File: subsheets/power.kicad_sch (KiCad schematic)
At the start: 27 parts

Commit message: Added MCU sch sheet and updated sheet layout
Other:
- company: (none) -> University of Central Florida
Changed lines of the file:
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@@
 (kicad_sch (version 20210621) (generator eeschema)
   (paper "A4")
-  (junction (at 172.72 55.88) (diameter 0) (color 0 0 0 0))
+  (title_block
+    (company "University of Central Florida")
+    (comment 1 "Randy Alvarez")
+    (comment 2 "Parke Benjamin")
+  )
+  (junction (at 115.57 62.23) (diameter 0) (color 0 0 0 0))
+  (junction (at 147.32 139.7) (diameter 0) (color 0 0 0 0))
+  (junction (at 69.85 72.39) (diameter 0) (color 0 0 0 0))
+  (junction (at 139.7 128.27) (diameter 0) (color 0 0 0 0))
+  (junction (at 115.57 88.9) (diameter 0) (color 0 0 0 0))
+  (junction (at 172.72 66.04) (diameter 0) (color 0 0 0 0))
   (junction (at 99.06 53.34) (diameter 0) (color 0 0 0 0))
-  (junction (at 172.72 66.04) (diameter 0) (color 0 0 0 0))
-  (junction (at 167.64 88.9) (diameter 0) (color 0 0 0 0))
+  (junction (at 113.03 88.9) (diameter 0) (color 0 0 0 0))
+  (junction (at 120.65 109.22) (diameter 0) (color 0 0 0 0))
+  (junction (at 77.47 72.39) (diameter 0) (color 0 0 0 0))
   (junction (at 91.44 53.34) (diameter 0) (color 0 0 0 0))
   (junction (at 186.69 88.9) (diameter 0) (color 0 0 0 0))
-  (junction (at 120.65 109.22) (diameter 0) (color 0 0 0 0))
+  (junction (at 167.64 88.9) (diameter 0) (color 0 0 0 0))
+  (junction (at 69.85 74.93) (diameter 0) (color 0 0 0 0))
   (junction (at 113.03 101.6) (diameter 0) (color 0 0 0 0))
-  (junction (at 115.57 88.9) (diameter 0) (color 0 0 0 0))
-  (junction (at 113.03 88.9) (diameter 0) (color 0 0 0 0))
-  (junction (at 139.7 128.27) (diameter 0) (color 0 0 0 0))
-  (junction (at 147.32 139.7) (diameter 0) (color 0 0 0 0))
-  (junction (at 77.47 72.39) (diameter 0) (color 0 0 0 0))
-  (junction (at 69.85 74.93) (diameter 0) (color 0 0 0 0))
+  (junction (at 165.1 58.42) (diameter 0) (color 0 0 0 0))
   (junction (at 120.65 114.3) (diameter 0) (color 0 0 0 0))
-  (junction (at 69.85 72.39) (diameter 0) (color 0 0 0 0))
+  (junction (at 172.72 55.88) (diameter 0) (color 0 0 0 0))
   (junction (at 217.17 55.88) (diameter 0) (color 0 0 0 0))
-  (junction (at 165.1 58.42) (diameter 0) (color 0 0 0 0))
-  (junction (at 115.57 62.23) (diameter 0) (color 0 0 0 0))
   (wire (pts (xy 59.69 77.47) (xy 57.15 77.47))
     (stroke (width 0) (type default) (color 0 0 0 0))

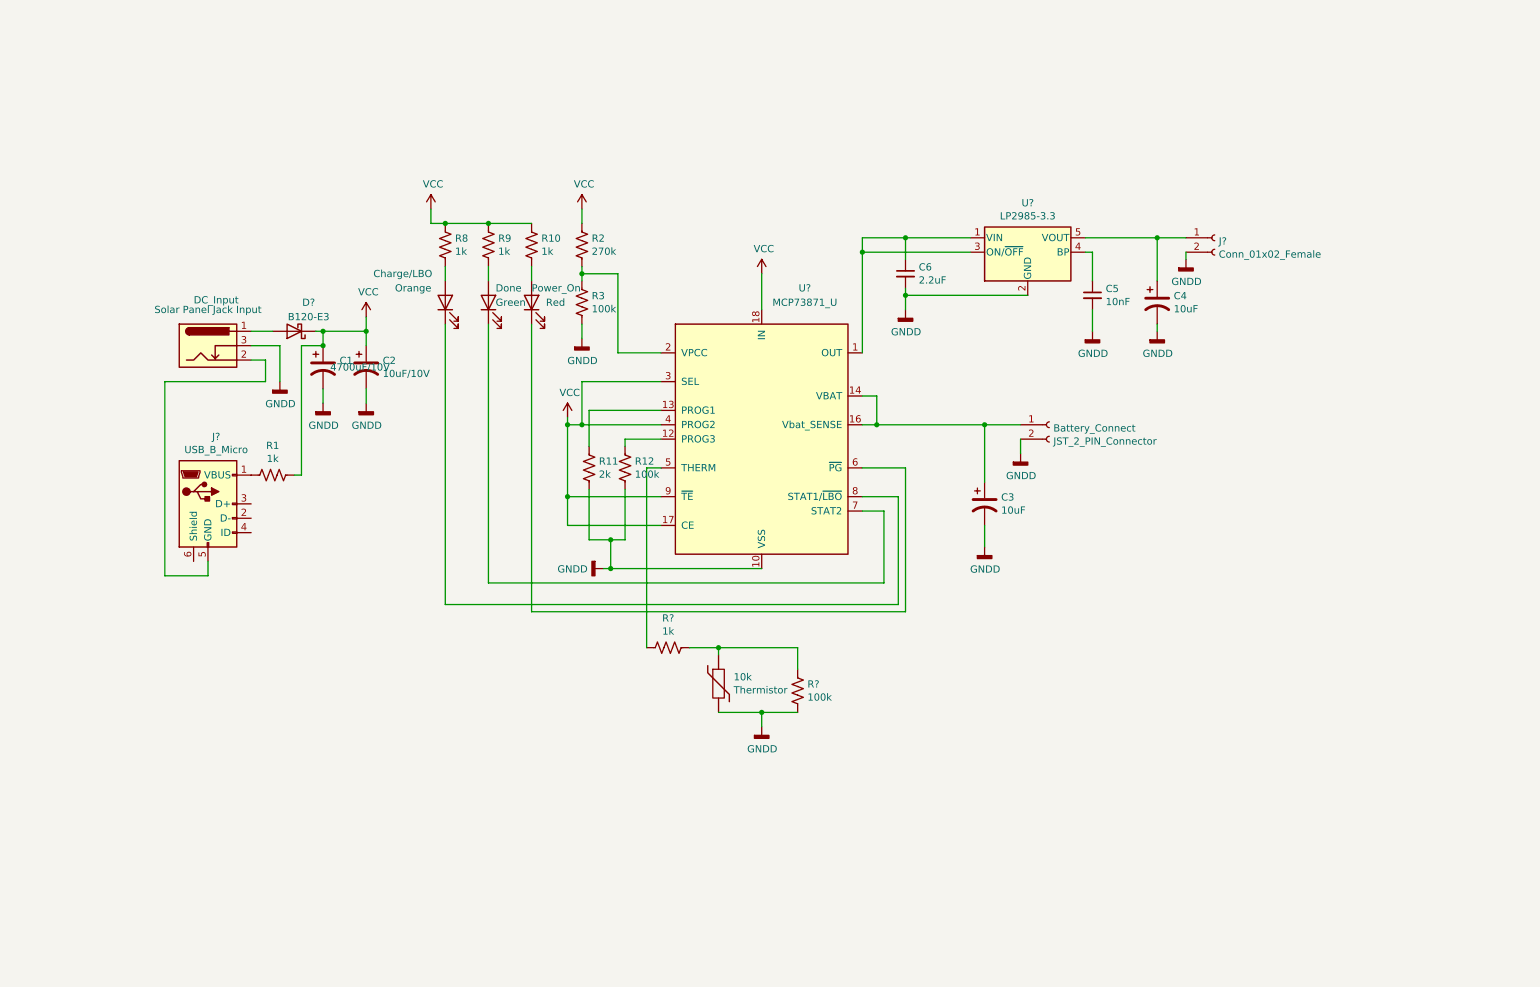
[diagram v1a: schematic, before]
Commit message: Created Sensor Library
- Added Bosch BME688, SPS30, ZMOD symbols to MCU schematic
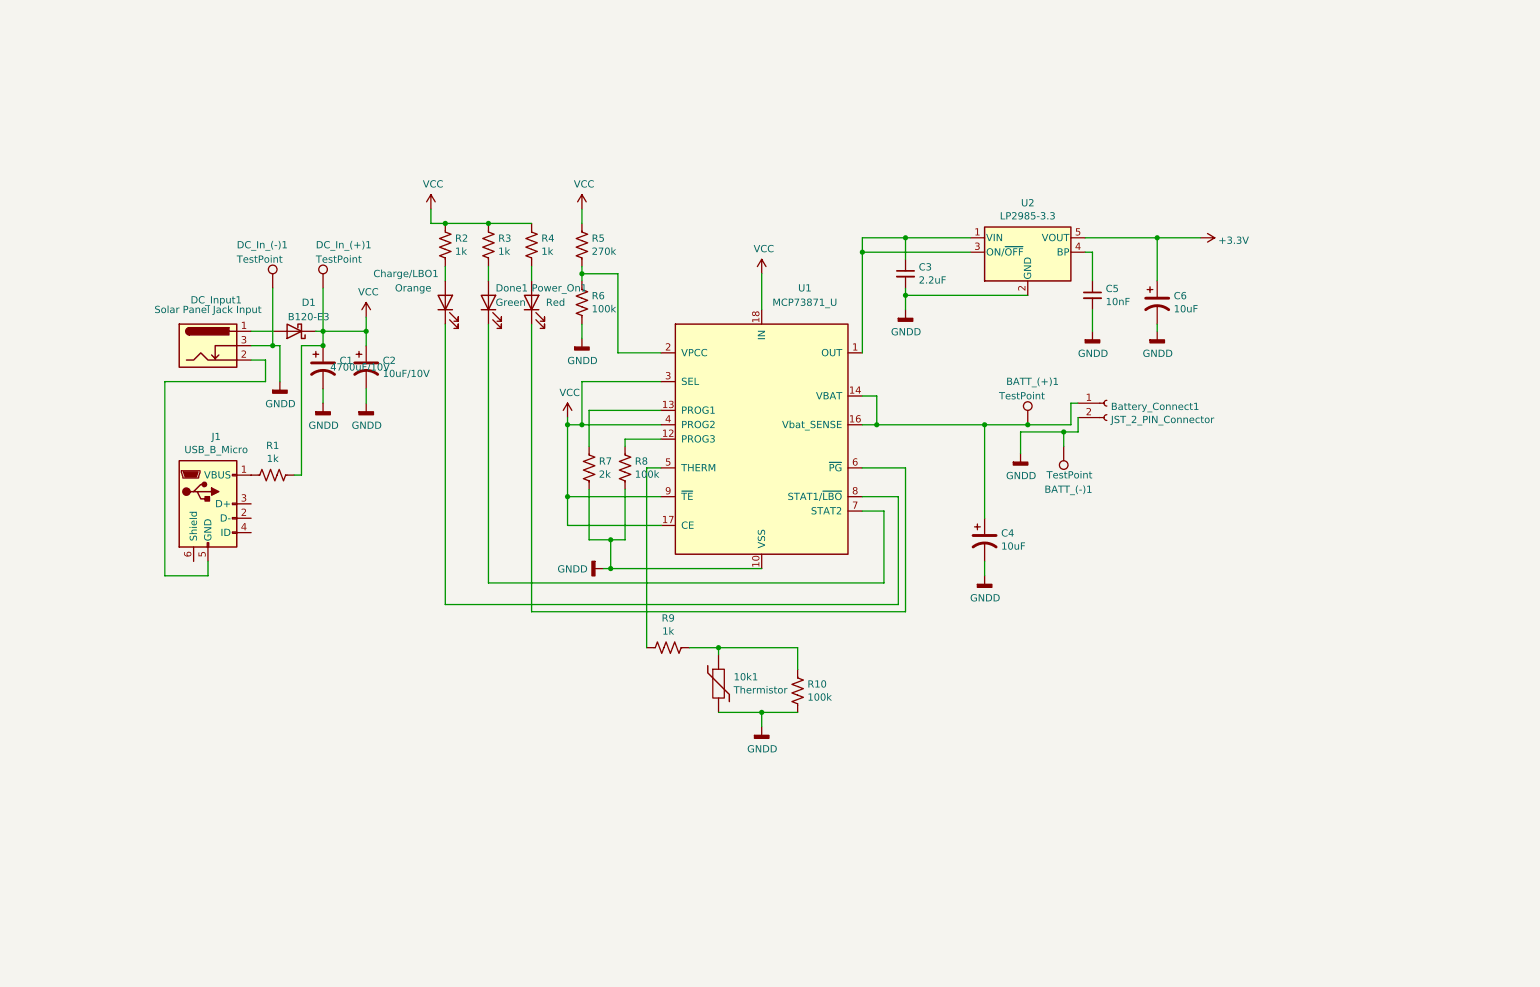
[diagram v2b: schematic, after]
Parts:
- removed J?: Conn_01x02_Female, symbol Connector:Conn_01x02_Female
- added BATT_(+)1, BATT_(-)1, DC_In_(+)1, DC_In_(-)1: TestPoint, symbol Connector:TestPoint
- gave numbers to parts that had none: 6
- renumbered 10k to 10k1, Battery_Connect to Battery_Connect1, C6 to C3, C3 to C4, C4 to C6, Charge/LBO to Charge/LBO1, DC_Input to DC_Input1, Done to Done1, Power_On to Power_On1, R8 to R2, R9 to R3, R10 to R4, R2 to R5, R3 to R6, R11 to R7, R12 to R8
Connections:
- net GNDD: now also BATT_(-)1.1, DC_In_(-)1.1
- net VCC: now also DC_In_(+)1.1
- net at Battery_Connect1.1 (Pin_1), C4.1, U1.14 (VBAT)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: now also BATT_(+)1.1
- net +3V3: now reaches C6.1, U2.5 (VOUT)
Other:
- moved on the sheet: Battery_Connect1, C4

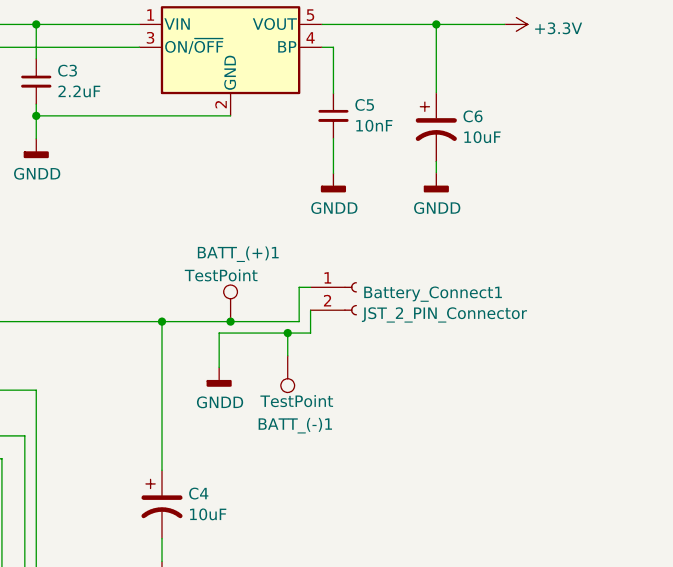
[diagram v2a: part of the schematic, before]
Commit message: Connected ZMOD and Bosch Sensors
-
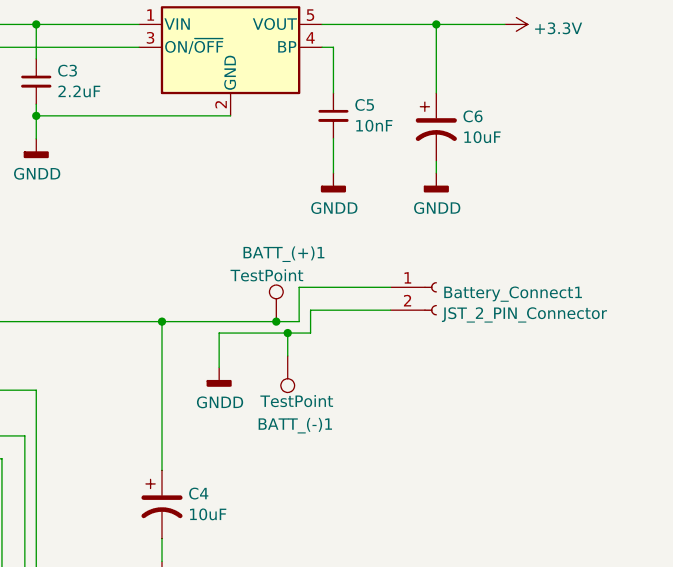
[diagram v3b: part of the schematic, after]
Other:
- moved on the sheet: BATT_(+)1, Battery_Connect1
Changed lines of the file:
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@@
     (comment 2 "Parke Benjamin")
   )
+  (junction (at 120.65 114.3) (diameter 0) (color 0 0 0 0))
+  (junction (at 69.85 72.39) (diameter 0) (color 0 0 0 0))
+  (junction (at 113.03 88.9) (diameter 0) (color 0 0 0 0))
+  (junction (at 200.66 90.17) (diameter 0) (color 0 0 0 0))
+  (junction (at 120.65 109.22) (diameter 0) (color 0 0 0 0))
+  (junction (at 115.57 62.23) (diameter 0) (color 0 0 0 0))
+  (junction (at 99.06 53.34) (diameter 0) (color 0 0 0 0))
+  (junction (at 115.57 88.9) (diameter 0) (color 0 0 0 0))
+  (junction (at 167.64 88.9) (diameter 0) (color 0 0 0 0))
+  (junction (at 77.47 72.39) (diameter 0) (color 0 0 0 0))
   (junction (at 69.85 74.93) (diameter 0) (color 0 0 0 0))
-  (junction (at 113.03 88.9) (diameter 0) (color 0 0 0 0))
-  (junction (at 217.17 55.88) (diameter 0) (color 0 0 0 0))
-  (junction (at 69.85 72.39) (diameter 0) (color 0 0 0 0))
+  (junction (at 172.72 55.88) (diameter 0) (color 0 0 0 0))
+  (junction (at 113.03 101.6) (diameter 0) (color 0 0 0 0))
   (junction (at 172.72 66.04) (diameter 0) (color 0 0 0 0))
-  (junction (at 115.57 88.9) (diameter 0) (color 0 0 0 0))
-  (junction (at 139.7 128.27) (diameter 0) (color 0 0 0 0))
-  (junction (at 120.65 109.22) (diameter 0) (color 0 0 0 0))
-  (junction (at 200.66 90.17) (diameter 0) (color 0 0 0 0))
-  (junction (at 172.72 55.88) (diameter 0) (color 0 0 0 0))
+  (junction (at 186.69 88.9) (diameter 0) (color 0 0 0 0))
+  (junction (at 199.39 88.9) (diameter 0) (color 0 0 0 0))
   (junction (at 165.1 58.42) (diameter 0) (color 0 0 0 0))
-  (junction (at 147.32 139.7) (diameter 0) (color 0 0 0 0))
-  (junction (at 99.06 53.34) (diameter 0) (color 0 0 0 0))
-  (junction (at 194.31 88.9) (diameter 0) (color 0 0 0 0))
-  (junction (at 115.57 62.23) (diameter 0) (color 0 0 0 0))
-  (junction (at 120.65 114.3) (diameter 0) (color 0 0 0 0))
-  (junction (at 186.69 88.9) (diameter 0) (color 0 0 0 0))
-  (junction (at 167.64 88.9) (diameter 0) (color 0 0 0 0))
   (junction (at 60.96 74.93) (diameter 0) (color 0 0 0 0))
   (junction (at 91.44 53.34) (diameter 0) (color 0 0 0 0))
-  (junction (at 113.03 101.6) (diameter 0) (color 0 0 0 0))
-  (junction (at 77.47 72.39) (diameter 0) (color 0 0 0 0))
+  (junction (at 147.32 139.7) (diameter 0) (color 0 0 0 0))
+  (junction (at 139.7 128.27) (diameter 0) (color 0 0 0 0))
+  (junction (at 217.17 55.88) (diameter 0) (color 0 0 0 0))
   (wire (pts (xy 59.69 77.47) (xy 57.15 77.47))
     (stroke (width 0) (type default) (color 0 0 0 0))
@@
     (stroke (width 0) (type default) (color 0 0 0 0))
   )
+  (wire (pts (xy 57.15 74.93) (xy 60.96 74.93))
+    (stroke (width 0) (type default) (color 0 0 0 0))
+  )
   (wire (pts (xy 60.96 74.93) (xy 62.23 74.93))
     (stroke (width 0) (type default) (color 0 0 0 0))
   )
-  (wire (pts (xy 57.15 74.93) (xy 60.96 74.93))
-    (stroke (width 0) (type default) (color 0 0 0 0))
-  )
-  (wire (pts (xy 201.93 85.09) (xy 203.2 85.09))
-    (stroke (width 0) (type default) (color 0 0 0 0))
-  )
-  (wire (pts (xy 194.31 88.9) (xy 201.93 88.9))
-    (stroke (width 0) (type default) (color 0 0 0 0))
-  )
   (wire (pts (xy 201.93 88.9) (xy 201.93 85.09))
     (stroke (width 0) (type default) (color 0 0 0 0))
   )
-  (wire (pts (xy 186.69 88.9) (xy 194.31 88.9))
+  (wire (pts (xy 201.93 85.09) (xy 212.09 85.09))
+    (stroke (width 0) (type default) (color 0 0 0 0))
+  )
+  (wire (pts (xy 186.69 88.9) (xy 199.39 88.9))
+    (stroke (width 0) (type default) (color 0 0 0 0))
+  )
+  (wire (pts (xy 199.39 88.9) (xy 201.93 88.9))
     (stroke (width 0) (type default) (color 0 0 0 0))
   )
@@
     (stroke (width 0) (type default) (color 0 0 0 0))
   )
+  (wire (pts (xy 115.57 88.9) (xy 113.03 88.9))
+    (stroke (width 0) (type default) (color 0 0 0 0))
+  )
   (wire (pts (xy 129.54 88.9) (xy 115.57 88.9))
     (stroke (width 0) (type default) (color 0 0 0 0))
   )
-  (wire (pts (xy 115.57 88.9) (xy 113.03 88.9))
-    (stroke (width 0) (type default) (color 0 0 0 0))
-  )
   (wire (pts (xy 217.17 55.88) (xy 224.79 55.88))
     (stroke (width 0) (type default) (color 0 0 0 0))
@@
     (stroke (width 0) (type default) (color 0 0 0 0))
   )
+  (wire (pts (xy 193.04 90.17) (xy 200.66 90.17))
+    (stroke (width 0) (type default) (color 0 0 0 0))
+  )
   (wire (pts (xy 203.2 90.17) (xy 203.2 87.63))
     (stroke (width 0) (type default) (color 0 0 0 0))
@@
     (stroke (width 0) (type default) (color 0 0 0 0))
   )
-  (wire (pts (xy 193.04 90.17) (xy 200.66 90.17))
-    (stroke (width 0) (type default) (color 0 0 0 0))
-  )
   (wire (pts (xy 165.1 83.82) (xy 167.64 83.82))
     (stroke (width 0) (type default) (color 0 0 0 0))
@@
   )
   (wire (pts (xy 69.85 64.77) (xy 69.85 72.39))
+    (stroke (width 0) (type default) (color 0 0 0 0))
+  )
+  (wire (pts (xy 203.2 87.63) (xy 212.09 87.63))
     (stroke (width 0) (type default) (color 0 0 0 0))
   )
@@
     (pin "3")
   )
-  (symbol (lib_id "Connector:Conn_01x02_Female") (at 208.28 85.09 0) (unit 1)
-    (in_bom yes) (on_board yes)
-    (property "Reference" "Battery_Connect1" (id 0) (at 208.9912 85.6996 0)
-      (effects (font (size 1.27 1.27)) (justify left))
-    )
-    (property "Value" "JST_2_PIN_Connector" (id 1) (at 208.9912 88.011 0)
-      (effects (font (size 1.27 1.27)) (justify left))
-    )
-    (property "Footprint" "" (id 2) (at 208.28 85.09 0)
-      (effects (font (size 1.27 1.27)) hide)
-    )
-    (property "Datasheet" "~" (id 3) (at 208.28 85.09 0)
+  (symbol (lib_id "Connector:Conn_01x02_Female") (at 217.17 85.09 0) (unit 1)
+    (in_bom yes) (on_board yes)
+    (property "Reference" "Battery_Connect1" (id 0) (at 217.8812 85.6996 0)
+      (effects (font (size 1.27 1.27)) (justify left))
+    )
+    (property "Value" "JST_2_PIN_Connector" (id 1) (at 217.8812 88.011 0)
+      (effects (font (size 1.27 1.27)) (justify left))
+    )
+    (property "Footprint" "" (id 2) (at 217.17 85.09 0)
+      (effects (font (size 1.27 1.27)) hide)
+    )
+    (property "Datasheet" "~" (id 3) (at 217.17 85.09 0)
       (effects (font (size 1.27 1.27)) hide)
     )
@@
     (pin "1")
   )
-  (symbol (lib_id "Connector:TestPoint") (at 194.31 88.9 0) (unit 1)
-    (in_bom yes) (on_board yes)
-    (property "Reference" "BATT_(+)1" (id 0) (at 190.5 81.28 0)
-      (effects (font (size 1.27 1.27)) (justify left))
-    )
-    (property "Value" "TestPoint" (id 1) (at 189.23 83.82 0)
-      (effects (font (size 1.27 1.27)) (justify left))
-    )
-    (property "Footprint" "" (id 2) (at 199.39 88.9 0)
-      (effects (font (size 1.27 1.27)) hide)
-    )
-    (property "Datasheet" "~" (id 3) (at 199.39 88.9 0)
-      (effects (font (size 1.27 1.27)) hide)
-    )
+  (symbol (lib_id "Connector:TestPoint") (at 199.39 88.9 0) (unit 1)
+    (in_bom yes) (on_board yes)
+    (property "Reference" "BATT_(+)1" (id 0) (at 195.58 81.28 0)
+      (effects (font (size 1.27 1.27)) (justify left))
+    )
+    (property "Value" "TestPoint" (id 1) (at 194.31 83.82 0)
+      (effects (font (size 1.27 1.27)) (justify left))
+    )
+    (property "Footprint" "" (id 2) (at 204.47 88.9 0)
+      (effects (font (size 1.27 1.27)) hide)
+    )
+    (property "Datasheet" "~" (id 3) (at 204.47 88.9 0)
+      (effects (font (size 1.27 1.27)) hide)
+    )
